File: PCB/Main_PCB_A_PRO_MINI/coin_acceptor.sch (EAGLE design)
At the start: 58 parts, among them J1 J15MM, J2 J10MM, J3 J15MM, Q1 IRF512, Q6 IRF512, Q7 IRF512, Q8 IRF512, T2 BC547, X2 22-23-2041

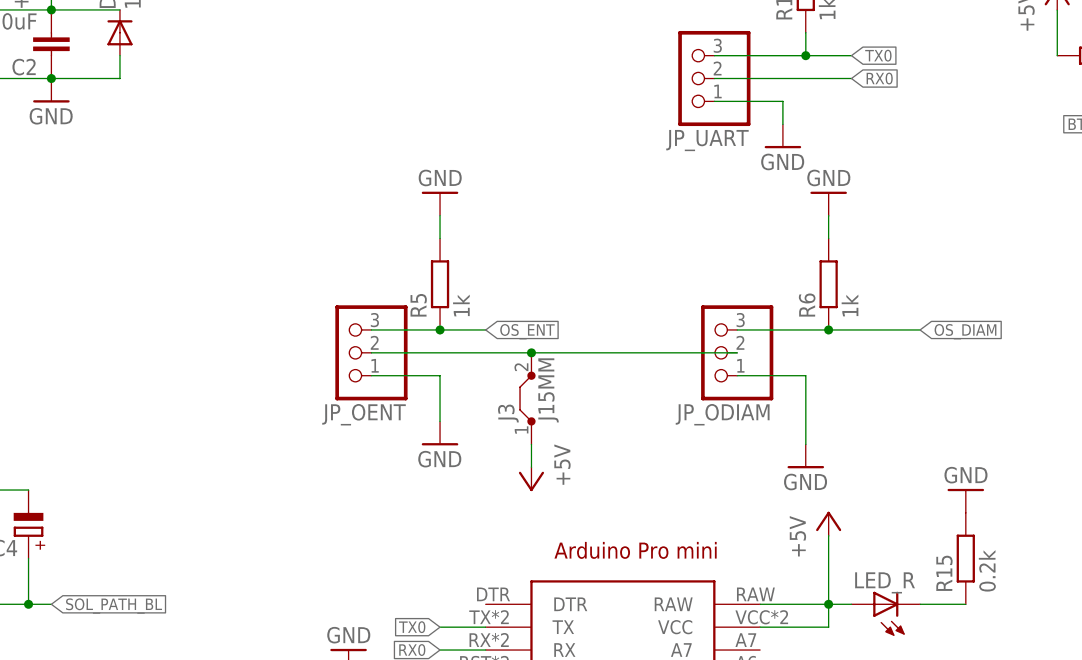
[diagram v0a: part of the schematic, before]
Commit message: Removed 5V direct output to optical block sensors. Removed pull-down resistors, and added .22k current protection resistors to optical sensor output.
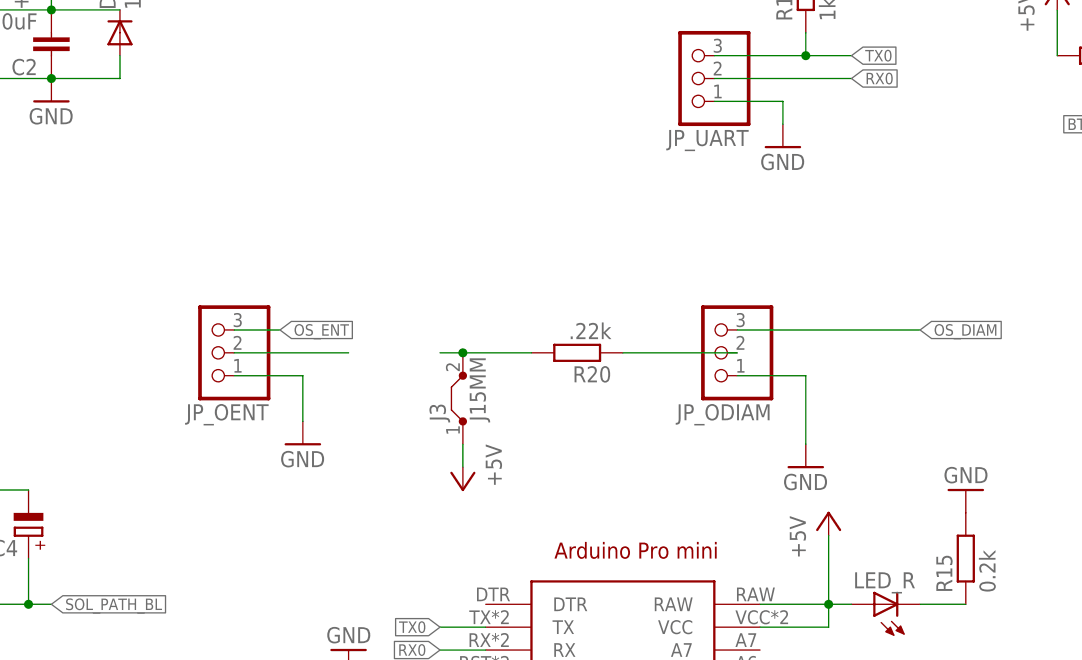
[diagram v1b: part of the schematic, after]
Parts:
- removed R5, R6: 1k, resistor:R-EU_0309/10
- added R20: .22k, resistor:R-EU_0309/10
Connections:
- new net N$8: JP_OENT.2
- new net N$9: JP_ODIAM.2, R20.1
- net GND: no longer R5.2, R6.2
- net N$5: now also R20.2; no longer JP_ODIAM.2, JP_OENT.2
- net OS_DIAM: no longer R6.1
- net OS_ENT: no longer R5.1
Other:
- moved on the sheet: J3, JP_OENT
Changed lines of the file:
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@@
 <part name="GND5" library="supply1" library_urn="urn:adsk.eagle:library:371" deviceset="GND" device=""/>
 <part name="JP_OENT" library="pinhead" library_urn="urn:adsk.eagle:library:325" deviceset="PINHD-1X3" device="" package3d_urn="urn:adsk.eagle:package:22458/2"/>
-<part name="R5" library="resistor" library_urn="urn:adsk.eagle:library:348" deviceset="R-EU_" device="0309/10" package3d_urn="urn:adsk.eagle:package:26087/1" value="1k"/>
 <part name="P+2" library="supply1" library_urn="urn:adsk.eagle:library:371" deviceset="+5V" device=""/>
 <part name="P+3" library="supply1" library_urn="urn:adsk.eagle:library:371" deviceset="+5V" device=""/>
 <part name="GND6" library="supply1" library_urn="urn:adsk.eagle:library:371" deviceset="GND" device=""/>
 <part name="JP_ODIAM" library="pinhead" library_urn="urn:adsk.eagle:library:325" deviceset="PINHD-1X3" device="" package3d_urn="urn:adsk.eagle:package:22458/2"/>
-<part name="R6" library="resistor" library_urn="urn:adsk.eagle:library:348" deviceset="R-EU_" device="0309/10" package3d_urn="urn:adsk.eagle:package:26087/1" value="1k"/>
 <part name="JP_ALRM" library="pinhead" library_urn="urn:adsk.eagle:library:325" deviceset="PINHD-1X2" device="" package3d_urn="urn:adsk.eagle:package:22435/2"/>
 <part name="JP_BAT_S" library="pinhead" library_urn="urn:adsk.eagle:library:325" deviceset="PINHD-1X2" device="" package3d_urn="urn:adsk.eagle:package:22435/2"/>
@@
 <part name="P+8" library="supply1" library_urn="urn:adsk.eagle:library:371" deviceset="+5V" device=""/>
 <part name="C2" library="rcl" library_urn="urn:adsk.eagle:library:334" deviceset="C-EU" device="025-024X044" package3d_urn="urn:adsk.eagle:package:23630/1" value="10uF"/>
-<part name="GND10" library="supply1" library_urn="urn:adsk.eagle:library:371" deviceset="GND" device=""/>
 <part name="JP_SEMP" library="pinhead" library_urn="urn:adsk.eagle:library:325" deviceset="PINHD-1X2" device="" package3d_urn="urn:adsk.eagle:package:22435/2"/>
 <part name="LED_G" library="led" library_urn="urn:adsk.eagle:library:259" deviceset="LED" device="5MM" package3d_urn="urn:adsk.eagle:package:15799/1"/>
@@
 <part name="R15" library="resistor" library_urn="urn:adsk.eagle:library:348" deviceset="R-EU_" device="0309/10" package3d_urn="urn:adsk.eagle:package:26087/1" value="0.2k"/>
 <part name="GND19" library="supply1" library_urn="urn:adsk.eagle:library:371" deviceset="GND" device=""/>
-<part name="GND20" library="supply1" library_urn="urn:adsk.eagle:library:371" deviceset="GND" device=""/>
 <part name="JP_12V" library="pinhead" library_urn="urn:adsk.eagle:library:325" deviceset="PINHD-1X2" device="" package3d_urn="urn:adsk.eagle:package:22435/2"/>
 <part name="P+5" library="supply1" library_urn="urn:adsk.eagle:library:371" deviceset="+12V" device=""/>
@@
 <part name="R18" library="resistor" library_urn="urn:adsk.eagle:library:348" deviceset="R-EU_" device="0309/10" package3d_urn="urn:adsk.eagle:package:26087/1" value="0.5k"/>
 <part name="R19" library="resistor" library_urn="urn:adsk.eagle:library:348" deviceset="R-EU_" device="0309/10" package3d_urn="urn:adsk.eagle:package:26087/1" value="0.5k"/>
+<part name="R20" library="resistor" library_urn="urn:adsk.eagle:library:348" deviceset="R-EU_" device="0309/10" package3d_urn="urn:adsk.eagle:package:26087/1" value=".22k"/>
 </parts>
 <sheets>
@@
 <instance part="JP_S_PTH" gate="G$1" x="132.08" y="-17.78" rot="R180"/>
 <instance part="GND4" gate="1" x="127" y="48.26" rot="R180"/>
-<instance part="GND5" gate="1" x="137.16" y="71.12"/>
-<instance part="JP_OENT" gate="A" x="127" y="81.28" rot="R180"/>
-<instance part="R5" gate="G$1" x="137.16" y="88.9" rot="R90"/>
-<instance part="P+2" gate="1" x="147.32" y="66.04" rot="R180"/>
+<instance part="GND5" gate="1" x="121.92" y="71.12"/>
+<instance part="JP_OENT" gate="A" x="111.76" y="81.28" rot="R180"/>
+<instance part="P+2" gate="1" x="139.7" y="66.04" rot="R180"/>
 <instance part="P+3" gate="1" x="180.34" y="63.5"/>
 <instance part="GND6" gate="1" x="177.8" y="68.58"/>
 <instance part="JP_ODIAM" gate="A" x="167.64" y="81.28" rot="R180"/>
-<instance part="R6" gate="G$1" x="180.34" y="88.9" rot="R90"/>
 <instance part="JP_ALRM" gate="G$1" x="88.9" y="-45.72" rot="R180"/>
 <instance part="JP_BAT_S" gate="G$1" x="132.08" y="-48.26" rot="R180"/>
@@
 <instance part="P+8" gate="1" x="93.98" y="124.46"/>
 <instance part="C2" gate="G$1" x="93.98" y="114.3" rot="R180"/>
-<instance part="GND10" gate="1" x="137.16" y="99.06" rot="R180"/>
 <instance part="JP_SEMP" gate="G$1" x="20.32" y="-60.96" rot="R180"/>
 <instance part="LED_G" gate="G$1" x="124.46" y="40.64" rot="R270"/>
@@
 <instance part="R15" gate="G$1" x="195.58" y="58.42" rot="R90"/>
 <instance part="GND19" gate="1" x="195.58" y="66.04" rot="R180"/>
-<instance part="GND20" gate="1" x="180.34" y="99.06" rot="R180"/>
 <instance part="JP_12V" gate="G$1" x="48.26" y="114.3" rot="R180"/>
 <instance part="P+5" gate="1" x="60.96" y="124.46"/>
@@
 <instance part="J1" gate="1" x="198.12" y="0" rot="R90"/>
 <instance part="J2" gate="1" x="38.1" y="-71.12" rot="R90"/>
-<instance part="J3" gate="1" x="147.32" y="76.2" rot="R90"/>
+<instance part="J3" gate="1" x="139.7" y="76.2" rot="R90"/>
 <instance part="B1" gate="1" x="124.46" y="12.7"/>
 <instance part="X2" gate="-1" x="231.14" y="114.3"/>
@@
 <instance part="R18" gate="G$1" x="210.82" y="114.3" rot="R180"/>
 <instance part="R19" gate="G$1" x="220.98" y="109.22" rot="R180"/>
+<instance part="R20" gate="G$1" x="152.4" y="81.28" rot="R180"/>
 </instances>
 <busses>
@@
 </segment>
 <segment>
-<pinref part="R6" gate="G$1" pin="1"/>
-<wire x1="180.34" y1="83.82" x2="190.5" y2="83.82" width="0.1524" layer="91"/>
 <label x="190.5" y="83.82" size="1.27" layer="95" xref="yes"/>
 <pinref part="JP_ODIAM" gate="A" pin="3"/>
-<wire x1="180.34" y1="83.82" x2="170.18" y2="83.82" width="0.1524" layer="91"/>
-<junction x="180.34" y="83.82"/>
+<wire x1="190.5" y1="83.82" x2="170.18" y2="83.82" width="0.1524" layer="91"/>
 </segment>
 </net>
@@
 </segment>
 <segment>
-<pinref part="R5" gate="G$1" pin="1"/>
-<wire x1="137.16" y1="83.82" x2="142.24" y2="83.82" width="0.1524" layer="91"/>
-<label x="142.24" y="83.82" size="1.27" layer="95" xref="yes"/>
+<label x="119.38" y="83.82" size="1.27" layer="95" xref="yes"/>
 <pinref part="JP_OENT" gate="A" pin="3"/>
-<wire x1="129.54" y1="83.82" x2="137.16" y2="83.82" width="0.1524" layer="91"/>
-<junction x="137.16" y="83.82"/>
+<wire x1="114.3" y1="83.82" x2="119.38" y2="83.82" width="0.1524" layer="91"/>
 </segment>
 </net>
@@
 <pinref part="JP_OENT" gate="A" pin="1"/>
 <pinref part="GND5" gate="1" pin="GND"/>
-<wire x1="129.54" y1="78.74" x2="137.16" y2="78.74" width="0.1524" layer="91"/>
-<wire x1="137.16" y1="78.74" x2="137.16" y2="73.66" width="0.1524" layer="91"/>
+<wire x1="114.3" y1="78.74" x2="121.92" y2="78.74" width="0.1524" layer="91"/>
+<wire x1="121.92" y1="78.74" x2="121.92" y2="73.66" width="0.1524" layer="91"/>
 </segment>
 <segment>
@@
 </segment>
 <segment>
-<pinref part="R5" gate="G$1" pin="2"/>
-<pinref part="GND10" gate="1" pin="GND"/>
-<wire x1="137.16" y1="93.98" x2="137.16" y2="96.52" width="0.1524" layer="91"/>
-</segment>
-<segment>
 <pinref part="R13" gate="G$1" pin="2"/>
 <pinref part="GND16" gate="1" pin="GND"/>
@@
 <pinref part="R15" gate="G$1" pin="2"/>
 <pinref part="GND19" gate="1" pin="GND"/>
-</segment>
-<segment>
-<pinref part="GND20" gate="1" pin="GND"/>
-<pinref part="R6" gate="G$1" pin="2"/>
-<wire x1="180.34" y1="96.52" x2="180.34" y2="93.98" width="0.1524" layer="91"/>
 </segment>
 <segment>
@@
 <pinref part="P+2" gate="1" pin="+5V"/>
 <pinref part="J3" gate="1" pin="1"/>
-<wire x1="147.32" y1="68.58" x2="147.32" y2="71.12" width="0.1524" layer="91"/>
+<wire x1="139.7" y1="68.58" x2="139.7" y2="71.12" width="0.1524" layer="91"/>
 </segment>
 <segment>
@@
 <net name="N$5" class="1">
 <segment>
-<pinref part="JP_OENT" gate="A" pin="2"/>
-<wire x1="129.54" y1="81.28" x2="147.32" y2="81.28" width="0.1524" layer="91"/>
 <pinref part="J3" gate="1" pin="2"/>
-<pinref part="JP_ODIAM" gate="A" pin="2"/>
-<wire x1="170.18" y1="81.28" x2="147.32" y2="81.28" width="0.1524" layer="91"/>
-<junction x="147.32" y="81.28"/>
+<wire x1="137.16" y1="81.28" x2="139.7" y2="81.28" width="0.1524" layer="91"/>
+<pinref part="R20" gate="G$1" pin="2"/>
+<wire x1="139.7" y1="81.28" x2="147.32" y2="81.28" width="0.1524" layer="91"/>
+<junction x="139.7" y="81.28"/>
 </segment>
 </net>
@@
 </segment>
 </net>
+<net name="N$8" class="0">
+<segment>
+<pinref part="JP_OENT" gate="A" pin="2"/>
+<wire x1="127" y1="81.28" x2="114.3" y2="81.28" width="0.1524" layer="91"/>
+</segment>
+</net>
+<net name="N$9" class="0">
+<segment>
+<pinref part="R20" gate="G$1" pin="1"/>
+<pinref part="JP_ODIAM" gate="A" pin="2"/>
+<wire x1="157.48" y1="81.28" x2="170.18" y2="81.28" width="0.1524" layer="91"/>
+</segment>
+</net>
